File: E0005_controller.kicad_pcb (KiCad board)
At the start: 4 copper layers, 125 x 65 mm, 270 parts, among them J1 SM04B-GHS-TB, J10 FH12-18S-0.5SH, J11 USB4105-GF-A, J12 SM02B-GHS-TB, J2 SM04B-GHS-TB, J3 SM04B-GHS-TB, J4 SM04B-GHS-TB, J5 SM06B-GHS-TB, J6 SM02B-GHS-TB, J7 SM02B-GHS-TB, J8 SM02B-GHS-TB, J9 SM02B-GHS-TB, Q1 PSMN2R0-30YLDX, Q11 2N7002, Q12 2N7002, Q13 AO3401A, Q14 2N7002, Q2 PSMN2R0-30YLDX, Q3 2N7002, Q4 2N7002, Q5 2N7002, Q6 2N7002, Q7 2N7002, SW1 PWR, SW2 BOOT, SW3 RESET, U1 ESP32-S3-WROOM-1-N16R2, U10 TPS259470ARPW, U11 TPS259470ARPW, U12 TPS259470ARPW, U13 TPS259470ARPW, U14 TPS259470ARPW, U15 MAX17205G+, U16 TPS259470ARPW, U17 TPS56637RPAR, U2 BQ25887RGER, U4 USBLC6-2SC6, U5 TPS629210DRL, U6 S-8252AAG-M6T1U, U8 PCA9548APW, U9 TCA9535PWR

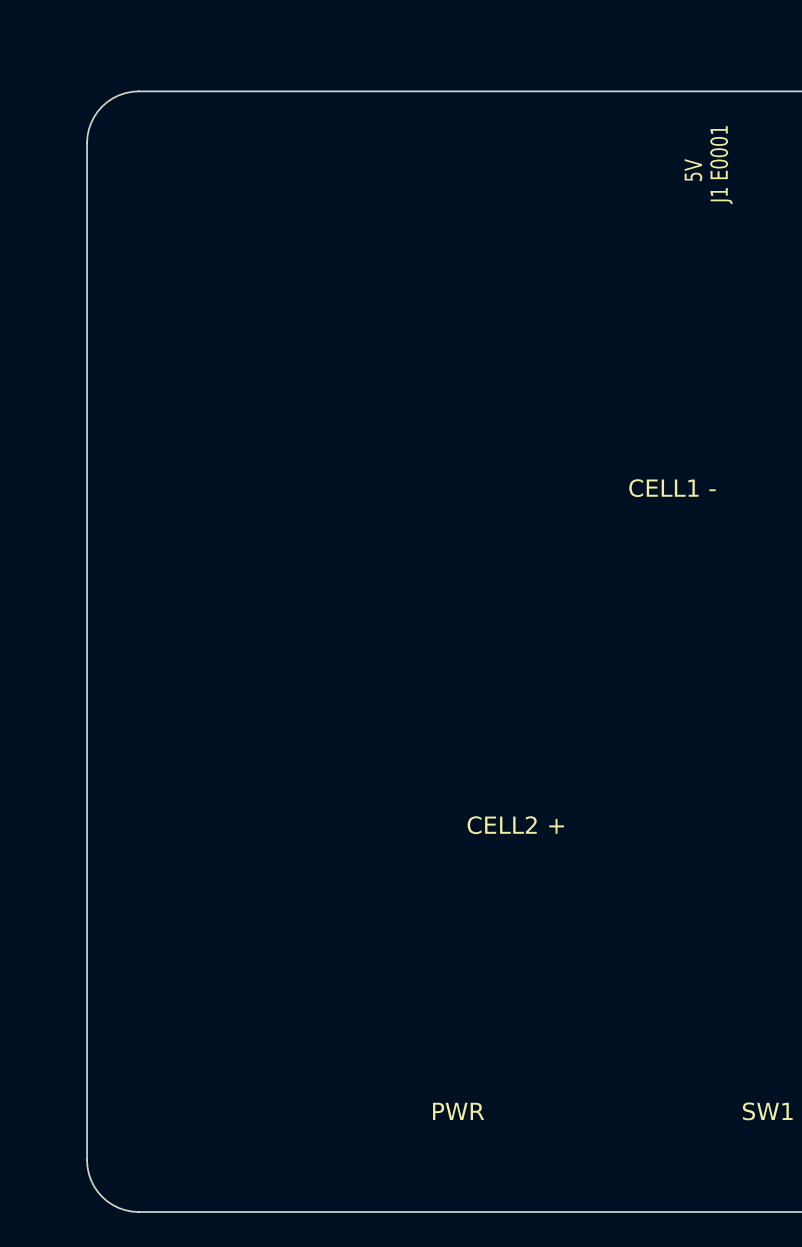
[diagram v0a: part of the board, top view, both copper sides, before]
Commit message: E0005 routing milestone 1: power stage (U16 U_IN pours, U17 buck hot loop, U2 charger loop/fan-out, U5 3V3); hand/IPC routing scripts in build/route
Co-Authored-By: Claude Opus 5.5 <noreply@anthropic.com>
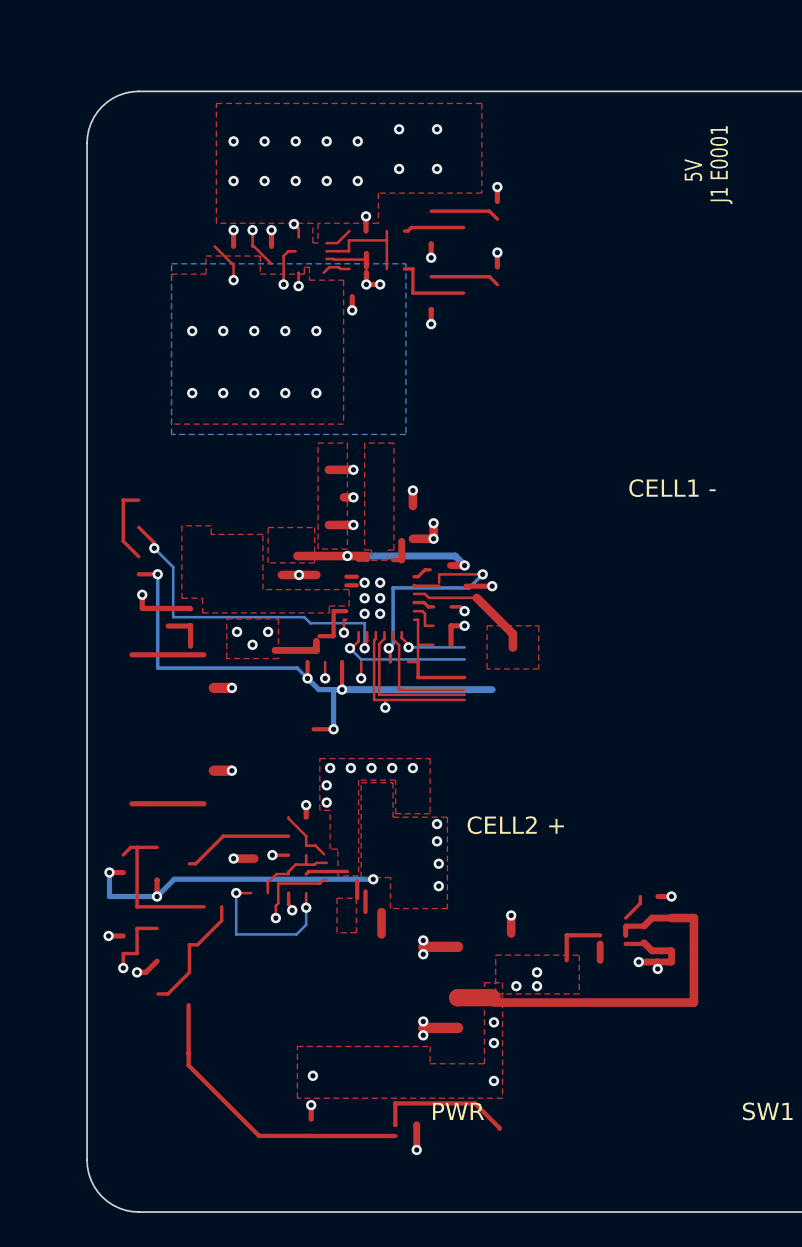
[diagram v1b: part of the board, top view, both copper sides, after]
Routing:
- net GND: track 0.00 -> 47.0 mm, vias 0 -> 44
- net +3V3: track 0.00 -> 35.9 mm, vias 0 -> 7
- net V5: track 0.00 -> 25.2 mm, vias 0 -> 20
- net /MCU, UI, LCD, switches/PB_RAW: track 0.00 -> 25.1 mm
- net BAT+: track 0.00 -> 22.5 mm, vias 0 -> 9
- net /Power: USB-C, U_IN, charger, 5 V buck, 3V3/CHG_STAT: track 0.00 -> 19.7 mm, vias 0 -> 2
- net /Power: USB-C, U_IN, charger, 5 V buck, 3V3/USB_SHIELD: track 0.00 -> 19.7 mm
- net CHG_CD: track 0.00 -> 15.4 mm, vias 0 -> 2
- net /Power: USB-C, U_IN, charger, 5 V buck, 3V3/REGN: track 0.00 -> 14.5 mm, vias 0 -> 2
- net /Power: USB-C, U_IN, charger, 5 V buck, 3V3/CHG_SW: track 0.00 -> 12.7 mm, vias 0 -> 2
- net Net-(Q13-G): track 0.00 -> 9.48 mm
- net Net-(C79-Pad1): track 0.00 -> 9.40 mm, vias 0 -> 2
- net VBUS: track 0.00 -> 9.23 mm, vias 0 -> 16
- net I2C0_SDA: track 0.00 -> 8.71 mm
- net CHG_PG_N: track 0.00 -> 8.15 mm, vias 0 -> 1
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- added copper zone on F.Cu, net +3V3
- added copper zone on F.Cu, net /Power: USB-C, U_IN, charger, 5 V buck, 3V3/BUCK_SW
- added copper zone on F.Cu, net /Power: USB-C, U_IN, charger, 5 V buck, 3V3/CHG_CBSET
- added copper zone on F.Cu, net /Power: USB-C, U_IN, charger, 5 V buck, 3V3/CHG_PMID
- added copper zone on F.Cu, net /Power: USB-C, U_IN, charger, 5 V buck, 3V3/CHG_SNS
- added copper zone on F.Cu, net /Power: USB-C, U_IN, charger, 5 V buck, 3V3/CHG_SW
- added copper zone on F.Cu, net BAT+
- added copper zone on In2.Cu, net BAT+
- added copper zone on F.Cu, net GND
- added copper zone on F.Cu, net V5
- added copper zone on B.Cu, net VBUS
- added copper zone on F.Cu, net VBUS
- added copper zone on In2.Cu, net VBUS

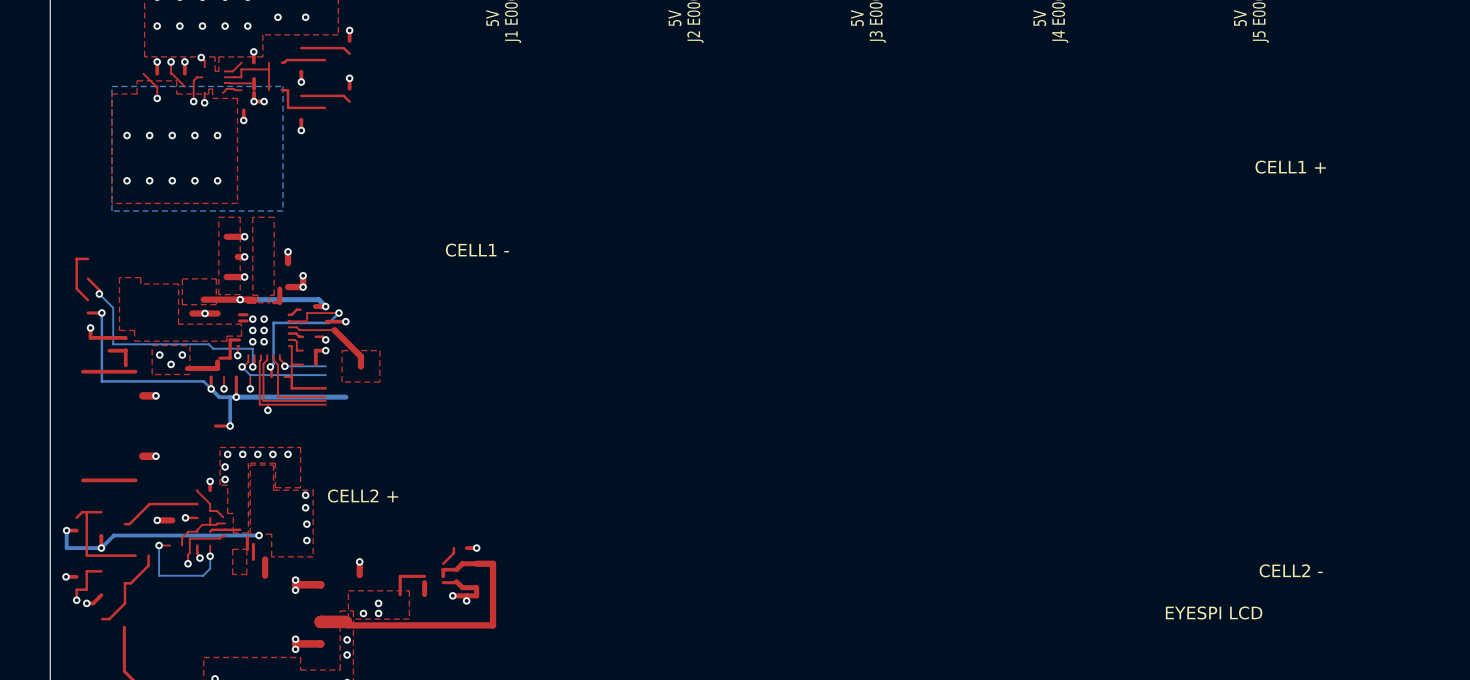
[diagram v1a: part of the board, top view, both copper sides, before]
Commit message: E0005 routing milestone 2: battery path (B_N/FET_D/SNS_P pours F.Cu+In2, CELL2_P, MID link B.Cu+In2, MID/CBSET sense traces from the lug), S-8252 and MAX17205 with Kelvin CSP/CSN from R20; nudges R28/R29/R30
Co-Authored-By: Claude Opus 5.5 <noreply@anthropic.com>
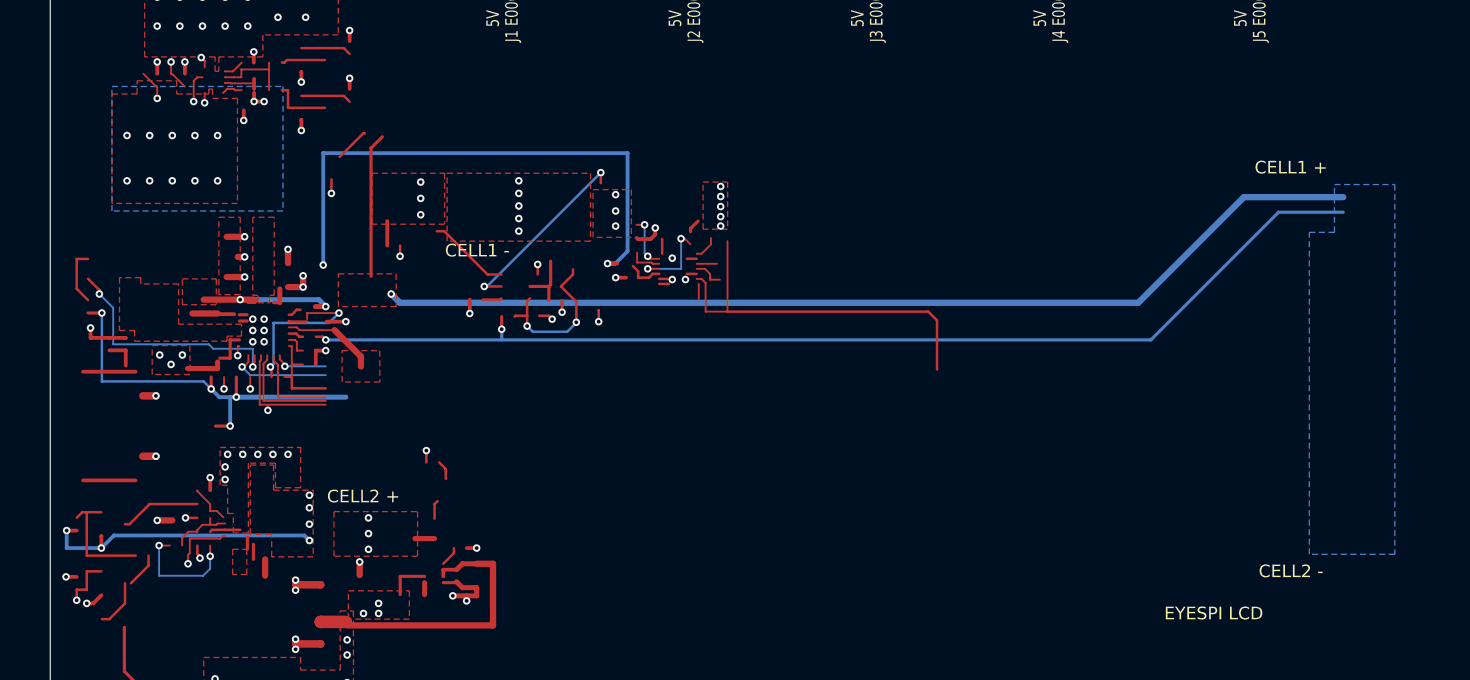
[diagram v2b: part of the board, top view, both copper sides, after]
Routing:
- net MID: track 0.89 -> 195.0 mm, vias 1 -> 4
- net BAT+: track 22.5 -> 70.4 mm, vias 9 -> 10
- net /Battery pack, protection, gauge/GAUGE_AIN1: track 0.00 -> 31.3 mm
- net /Battery pack, protection, gauge/B_N: track 0.00 -> 29.1 mm, vias 0 -> 6
- net /Battery pack, protection, gauge/CELL2_P: track 0.00 -> 27.1 mm, vias 0 -> 4
- net /Battery pack, protection, gauge/CHG_G: track 0.00 -> 15.2 mm, vias 0 -> 2
- net /Battery pack, protection, gauge/S8252_VC: track 0.00 -> 12.9 mm, vias 0 -> 2
- net Net-(D5-A): track 0.00 -> 10.9 mm, vias 0 -> 2
- net GND: track 47.0 -> 57.2 mm, vias 44 -> 54
- net /Battery pack, protection, gauge/GAUGE_CSN: track 0.00 -> 6.90 mm, vias 0 -> 2
- net /Battery pack, protection, gauge/DSG_G: track 0.00 -> 6.56 mm
- net /Battery pack, protection, gauge/S8252_VDD: track 0.00 -> 4.70 mm
- net SNS_P: track 0.00 -> 4.25 mm, vias 0 -> 5
- net /Battery pack, protection, gauge/GAUGE_VBATT: track 0.00 -> 2.89 mm
- net Net-(D5-K): track 0.00 -> 2.79 mm
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- added copper zone on F.Cu, net /Battery pack, protection, gauge/B_N
- added copper zone on In2.Cu, net /Battery pack, protection, gauge/B_N
- added copper zone on F.Cu, net /Battery pack, protection, gauge/CELL2_P
- added copper zone on In2.Cu, net /Battery pack, protection, gauge/CELL2_P
- added copper zone on F.Cu, net /Battery pack, protection, gauge/FET_D
- added copper zone on In2.Cu, net /Battery pack, protection, gauge/FET_D
- added copper zone on B.Cu, net MID
- added copper zone on F.Cu, net MID
- added copper zone on In2.Cu, net MID
- added copper zone on F.Cu, net SNS_P
- added copper zone on In2.Cu, net SNS_P

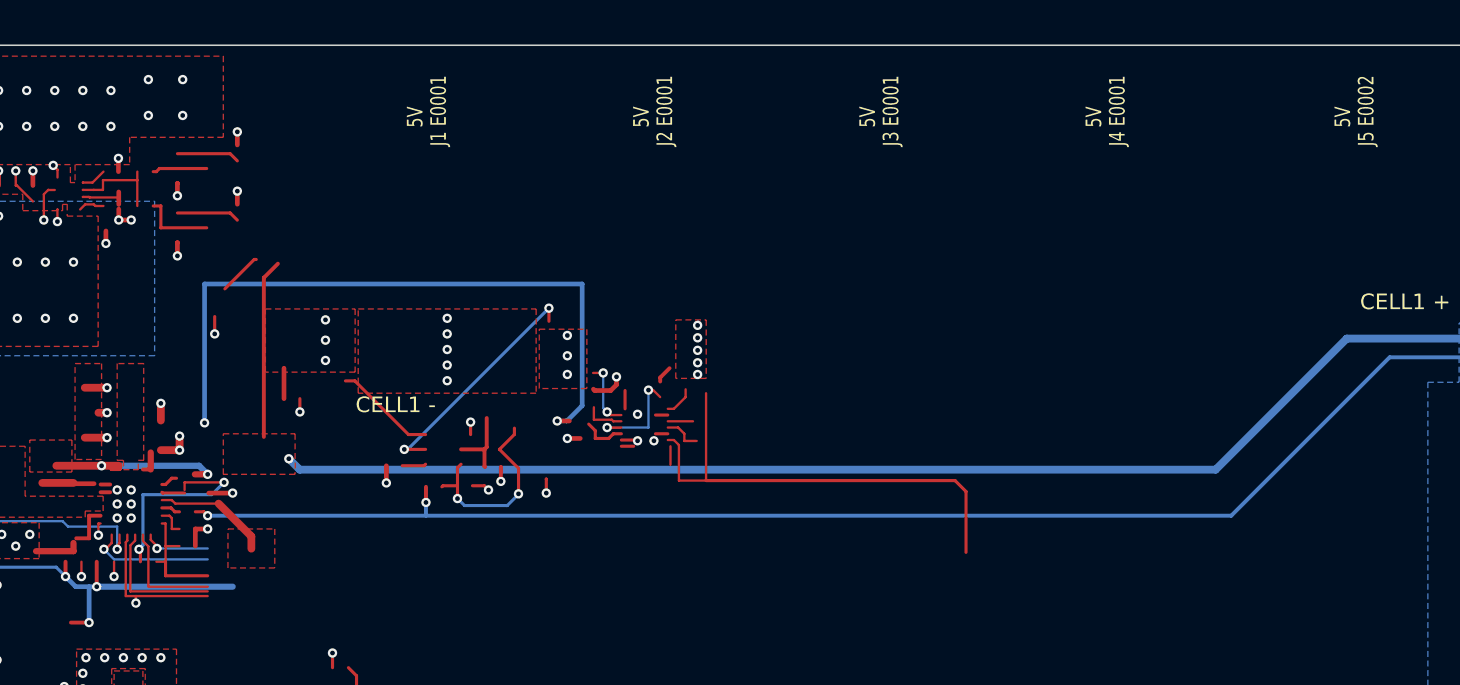
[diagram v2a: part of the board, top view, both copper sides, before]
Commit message: E0005 routing: port eFuses U10-U14 local routing (EN trees on In2, V5_k pours, ESD/connector), In2 split V5/3V3; nudges R98, R85
Co-Authored-By: Claude Opus 5.5 <noreply@anthropic.com>
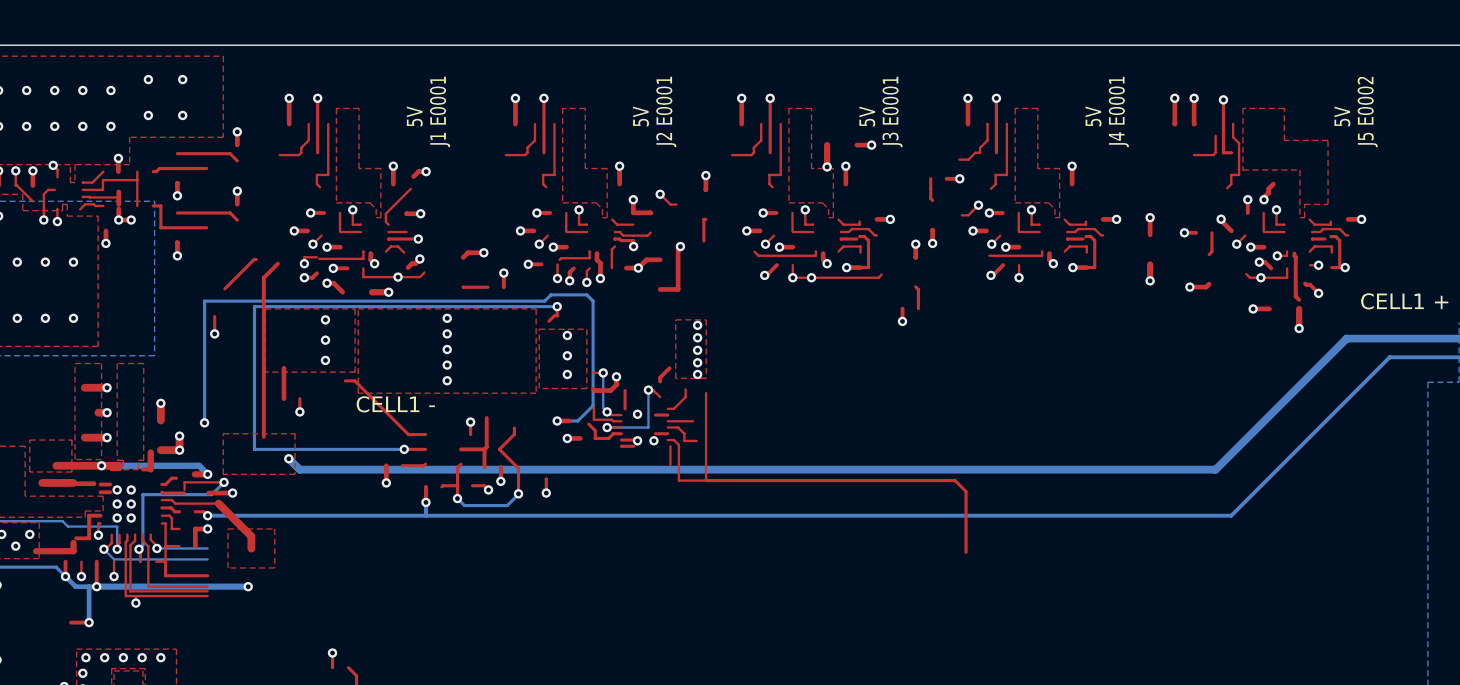
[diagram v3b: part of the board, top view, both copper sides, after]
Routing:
- net GND: track 57.2 -> 136.2 mm, vias 54 -> 102
- net /Battery pack, protection, gauge/CHG_G: track 15.2 -> 40.8 mm
- net V5: track 25.2 -> 50.1 mm, vias 20 -> 39
- net /I2C mux, expander, 5 V peripheral ports/PORT2_EN: track 0.00 -> 24.7 mm, vias 0 -> 4
- net /I2C mux, expander, 5 V peripheral ports/PORT1_EN: track 0.00 -> 17.9 mm, vias 0 -> 3
- net /I2C mux, expander, 5 V peripheral ports/PORT3_EN: track 0.00 -> 17.0 mm, vias 0 -> 4
- net /I2C mux, expander, 5 V peripheral ports/PORT4_EN: track 0.00 -> 14.6 mm, vias 0 -> 4
- net /I2C mux, expander, 5 V peripheral ports/PORT5_EN: track 0.00 -> 11.8 mm, vias 0 -> 3
- net +3V3: track 35.9 -> 43.1 mm, vias 7 -> 15
- net /I2C mux, expander, 5 V peripheral ports/PORT4_SCL_C: track 0.00 -> 4.99 mm
- net /I2C mux, expander, 5 V peripheral ports/PORT5_SCL_C: track 0.00 -> 4.89 mm
- net /I2C mux, expander, 5 V peripheral ports/PORT2_SCL_C: track 0.00 -> 4.86 mm
- net /I2C mux, expander, 5 V peripheral ports/PORT1_SCL_C: track 0.00 -> 4.86 mm
- net /I2C mux, expander, 5 V peripheral ports/PORT3_SCL_C: track 0.00 -> 4.86 mm
- net /I2C mux, expander, 5 V peripheral ports/PORT5_FLT_N: track 0.00 -> 4.70 mm, vias 0 -> 2
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- added copper zone on In2.Cu, net +3V3
- added copper zone on F.Cu, net /I2C mux, expander, 5 V peripheral ports/V5_1
- added copper zone on F.Cu, net /I2C mux, expander, 5 V peripheral ports/V5_2
- added copper zone on F.Cu, net /I2C mux, expander, 5 V peripheral ports/V5_3
- added copper zone on F.Cu, net /I2C mux, expander, 5 V peripheral ports/V5_4
- added copper zone on F.Cu, net /I2C mux, expander, 5 V peripheral ports/V5_5
- added copper zone on In1.Cu, net GND
- added copper zone on In2.Cu, net V5
